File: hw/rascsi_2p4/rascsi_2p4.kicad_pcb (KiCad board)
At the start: 2 copper layers, 65 x 56 mm, 98 parts, among them IC1 SN74LS641-1DW, IC2 SN74LS641-1DW, IC3 SN74LS641-1DW, IC4 SN74LS641-1DW, J1 Raspberry_Pi_2_3, J10 Conn_01x04_Male, J2 DNP, J20 171826-4, J3 Conn_02x25_Odd_Even, J4 I2C Pinout, J5 DNP, J6 CONNFLY DB-25, J7 DNP, J8 USB_B_Micro, J9 Conn_02x25_Odd_Even, X1 Mac, X2 Dogcow, X3 Mac, X4 Dogcow, X5 Dogcow, X6 Dogcow, X7 Pi, X8 Pi

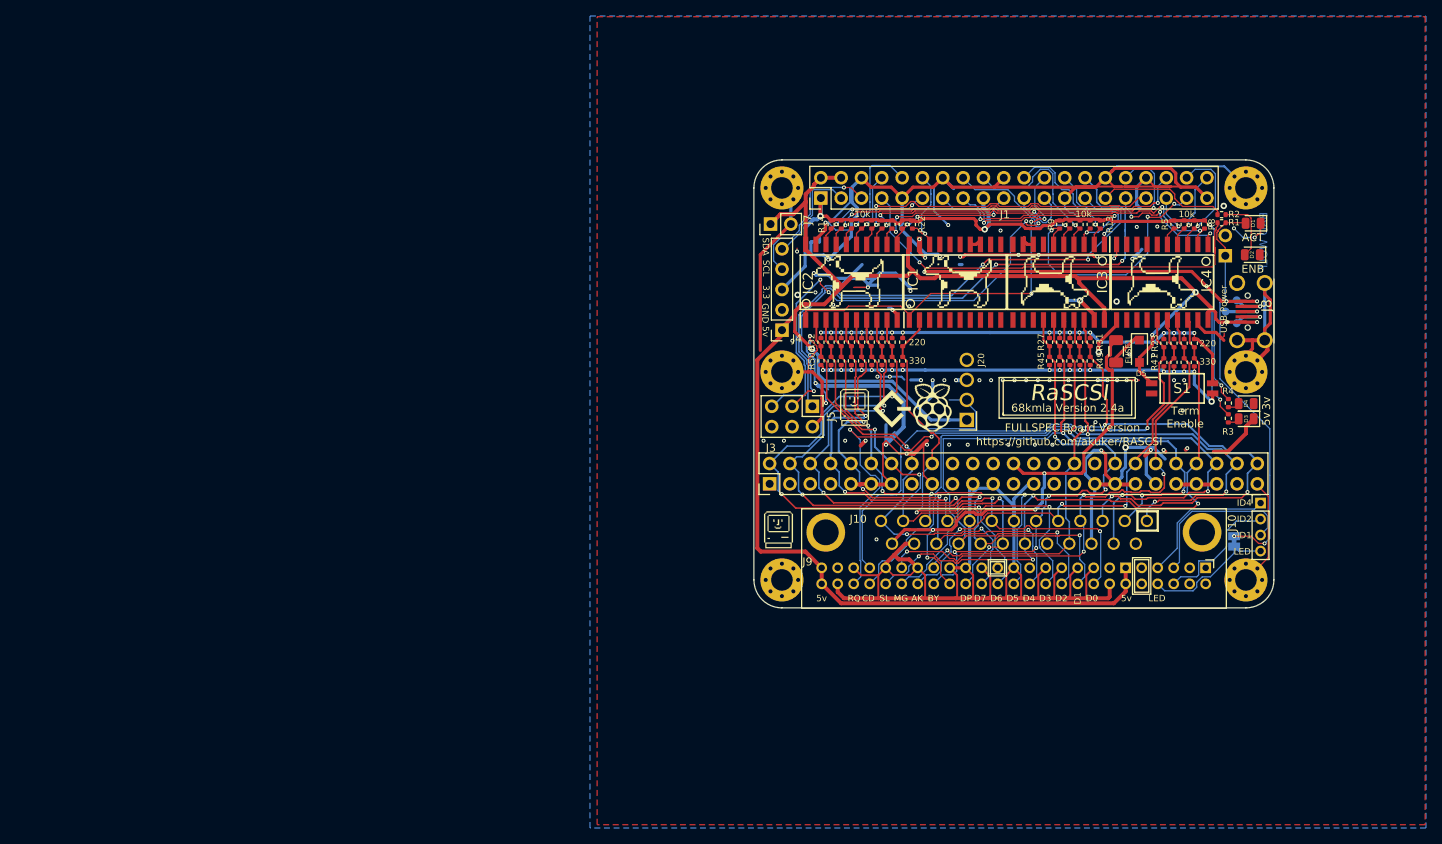
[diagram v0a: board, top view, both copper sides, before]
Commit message: replaced 4x74LS641 by 2x74ALVC164245DGG added pulldowns for floating in/out pins (instead of directly wiring them to ground) setup for autorouting
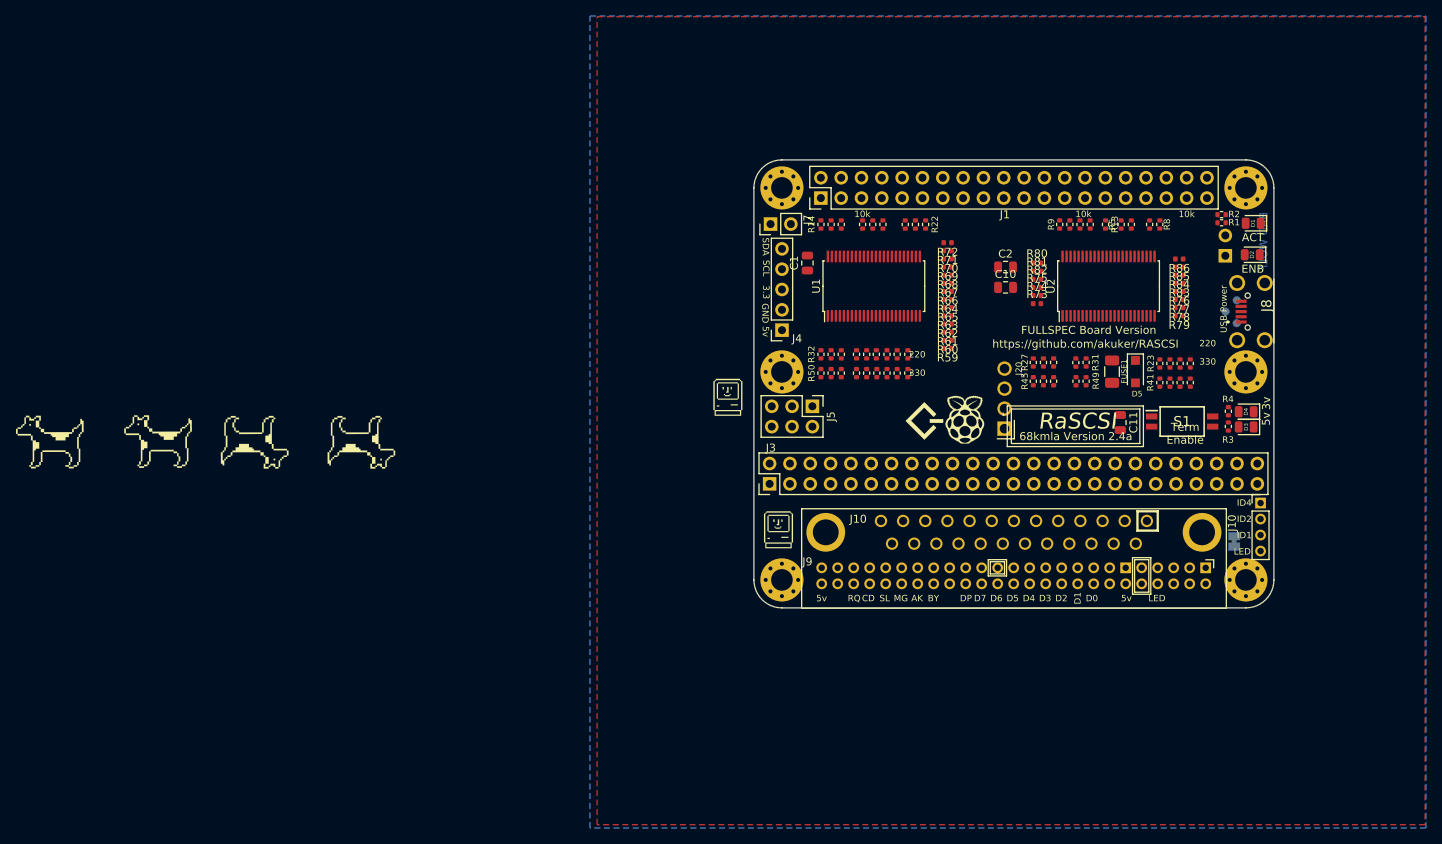
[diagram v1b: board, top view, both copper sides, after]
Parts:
- removed IC1, IC2, IC3, IC4: SN74LS641-1DW, SamacSys_Parts:SOIC127P1030X265-20N
- added C1: 330n, Capacitor_SMD:C_0805_2012Metric, F.Cu at (181.2, 55.4)
- added C10: 10u, Capacitor_SMD:C_0805_2012Metric, F.Cu at (206.0, 58.4)
- added C11: 10u, Capacitor_SMD:C_0805_2012Metric, F.Cu at (220.3, 75.3)
- added C2: 330n, Capacitor_SMD:C_0805_2012Metric, F.Cu at (206.0, 55.9)
- added R59: 10k, Resistor_SMD:R_0402_1005Metric, F.Cu at (198.7, 66.1)
- added R60: 10k, Resistor_SMD:R_0402_1005Metric, F.Cu at (198.7, 65.0)
- added R61: 10k, Resistor_SMD:R_0402_1005Metric, F.Cu at (198.7, 64.0)
- added R62: 10k, Resistor_SMD:R_0402_1005Metric, F.Cu at (198.7, 63.0)
- added R63: 10k, Resistor_SMD:R_0402_1005Metric, F.Cu at (198.7, 62.0)
- added R64: 10k, Resistor_SMD:R_0402_1005Metric, F.Cu at (198.7, 60.0)
- added R65: 10k, Resistor_SMD:R_0402_1005Metric, F.Cu at (198.7, 61.0)
- added R66: 10k, Resistor_SMD:R_0402_1005Metric, F.Cu at (198.7, 58.9)
- added R67: 10k, Resistor_SMD:R_0402_1005Metric, F.Cu at (198.7, 57.9)
- added R68: 10k, Resistor_SMD:R_0402_1005Metric, F.Cu at (198.7, 56.9)
- added R69: 10k, Resistor_SMD:R_0402_1005Metric, F.Cu at (198.7, 55.9)
- added R70: 10k, Resistor_SMD:R_0402_1005Metric, F.Cu at (198.7, 54.9)
- added R71: 10k, Resistor_SMD:R_0402_1005Metric, F.Cu at (198.7, 53.9)
- added R72: 10k, Resistor_SMD:R_0402_1005Metric, F.Cu at (198.7, 52.8)
- added R73: 10k, Resistor_SMD:R_0402_1005Metric, F.Cu at (209.9, 60.5)
- added R74: 10k, Resistor_SMD:R_0402_1005Metric, F.Cu at (209.9, 59.5)
- added R75: 10k, Resistor_SMD:R_0402_1005Metric, F.Cu at (209.9, 58.4)
- added R76: 10k, Resistor_SMD:R_0402_1005Metric, F.Cu at (227.7, 58.9)
- added R77: 10k, Resistor_SMD:R_0402_1005Metric, F.Cu at (227.7, 60.0)
- added R78: 10k, Resistor_SMD:R_0402_1005Metric, F.Cu at (227.7, 61.0)
- added R79: 10k, Resistor_SMD:R_0402_1005Metric, F.Cu at (227.7, 62.0)
- added R80: 10k, Resistor_SMD:R_0402_1005Metric, F.Cu at (209.9, 55.4)
- added R81: 10k, Resistor_SMD:R_0402_1005Metric, F.Cu at (209.9, 56.4)
- added R82: 10k, Resistor_SMD:R_0402_1005Metric, F.Cu at (209.9, 57.4)
- added R83: 10k, Resistor_SMD:R_0402_1005Metric, F.Cu at (227.7, 57.9)
- added R84: 10k, Resistor_SMD:R_0402_1005Metric, F.Cu at (227.7, 56.9)
- added R85: 10k, Resistor_SMD:R_0402_1005Metric, F.Cu at (227.7, 55.9)
- added R86: 10k, Resistor_SMD:R_0402_1005Metric, F.Cu at (227.7, 54.9)
- added U1: 74ALVC164245DGG, Package_SO:TSSOP-48_6.1x12.5mm_P0.5mm, F.Cu at (189.5, 58.3)
- added U2: 74ALVC164245DGG, Package_SO:TSSOP-48_6.1x12.5mm_P0.5mm, F.Cu at (218.8, 58.3)
- moved X2 102.0 mm to (86.5, 77.8)
- moved X4 102.0 mm to (125.4, 77.8)
- moved X5 102.0 mm to (112.1, 77.8)
- moved X6 102.0 mm to (100.0, 77.7)
- moved X3 15.9 mm to (171.3, 72.2)
- moved R5 6.60 mm to (220.4, 50.6)
- moved R6 6.60 mm to (221.7, 50.6)
- moved R7 5.59 mm to (224.0, 50.6)
- moved R8 5.59 mm to (225.2, 50.6)
- moved J20 4.84 mm to (205.8, 76.1)
- moved X7 4.34 mm to (200.9, 75.0)
- moved X8 4.34 mm to (195.7, 75.1)
- moved S1 4.14 mm to (228.0, 75.2)
- moved R45 3.25 mm to (209.4, 70.2)
- moved R47 3.25 mm to (212.0, 70.2)
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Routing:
- net GND: track 643.5 -> 0.00 mm, vias 80 -> 0
- net +5V: track 247.2 -> 0.00 mm, vias 6 -> 0
- net C-I_O: track 107.6 -> 0.00 mm, vias 3 -> 0
- net C-REQ: track 106.4 -> 0.00 mm, vias 5 -> 0
- net C-C_D: track 97.2 -> 0.00 mm, vias 3 -> 0
- net +3V3: track 95.2 -> 0.00 mm, vias 4 -> 0
- net C-D0: track 86.8 -> 0.00 mm, vias 4 -> 0
- net C-MSG: track 83.0 -> 0.00 mm, vias 3 -> 0
- net C-D1: track 81.5 -> 0.00 mm, vias 4 -> 0
- net C-SEL: track 76.2 -> 0.00 mm, vias 4 -> 0
- net C-D2: track 74.6 -> 0.00 mm, vias 4 -> 0
- net PI_GPIO1: track 71.8 -> 0.00 mm, vias 3 -> 0
- net /TERM_GND: track 69.1 -> 0.00 mm, vias 19 -> 0
- net C-D3: track 68.8 -> 0.00 mm, vias 4 -> 0
- net /TERM_5v: track 68.0 -> 0.00 mm, vias 18 -> 0
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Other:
- net class Power added: clearance 0.127, trace_width 0.6, via_dia 1, via_drill 0.6
